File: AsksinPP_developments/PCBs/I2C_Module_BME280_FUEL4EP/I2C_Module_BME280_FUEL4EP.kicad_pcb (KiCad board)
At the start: 2 copper layers, 30.5 x 17 mm, 12 parts, among them J1 Conn_01x04, J2 Conn_01x04, U1 BME280

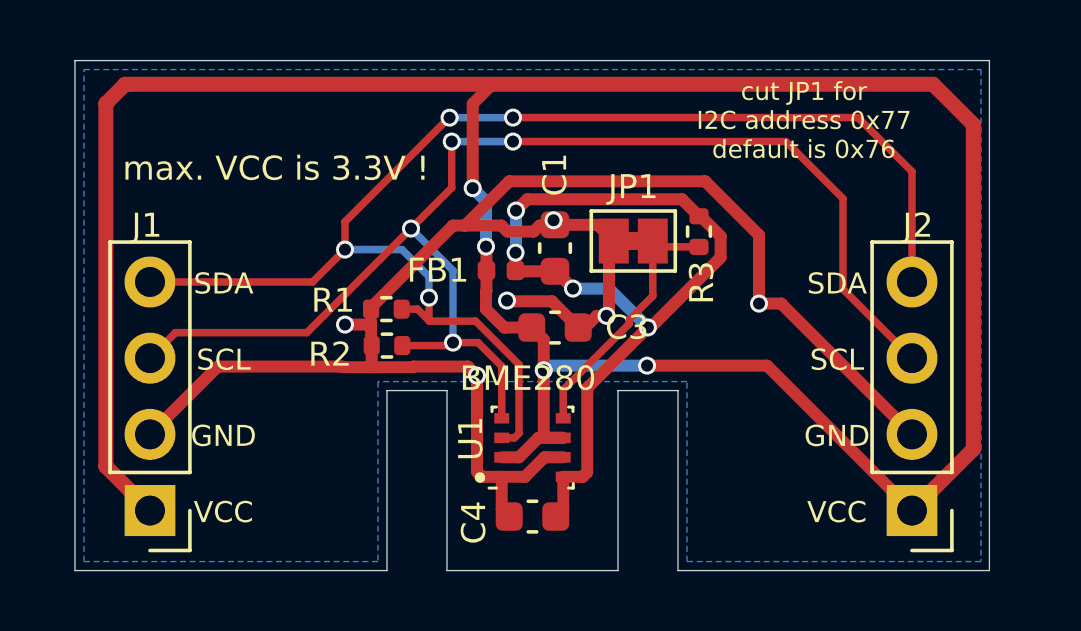
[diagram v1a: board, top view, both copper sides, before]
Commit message: PCB: I2C_Module_SHT85_BME280_FUEL4EP, I2C_Module_BME680_FUEL4EP: correction of connector placements in 3D view; 4Bit_I2C_Port_Expander_Module_FUEL4EP: change from 2N7000 to 2N7002K for SMD assembly
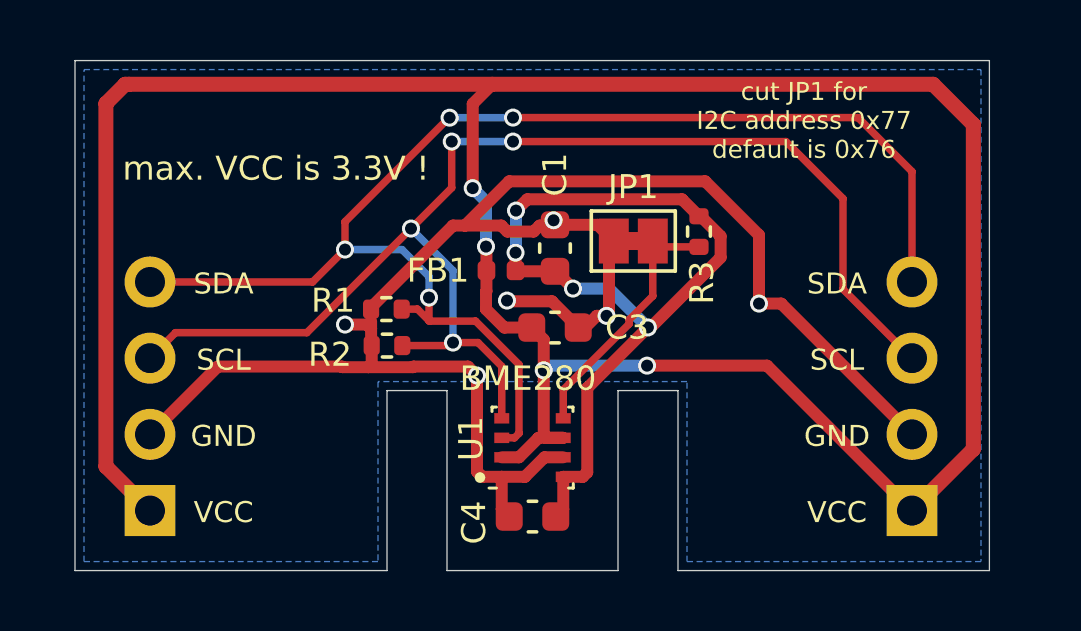
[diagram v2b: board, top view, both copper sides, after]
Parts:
- J1, J2: moved to B.Cu
- turned J1 to 0 degrees
- turned J2 to 0 degrees
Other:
- board text added: "BME280 I2C Modul (C) FUEL4EP V1.1 12/2023"
- board text removed: "BME280 I2C Modul (C) FUEL4EP V1.0 9/2023"

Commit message: PCBs: fix of I2C Pull-up resistors that were wrongly tied to GND
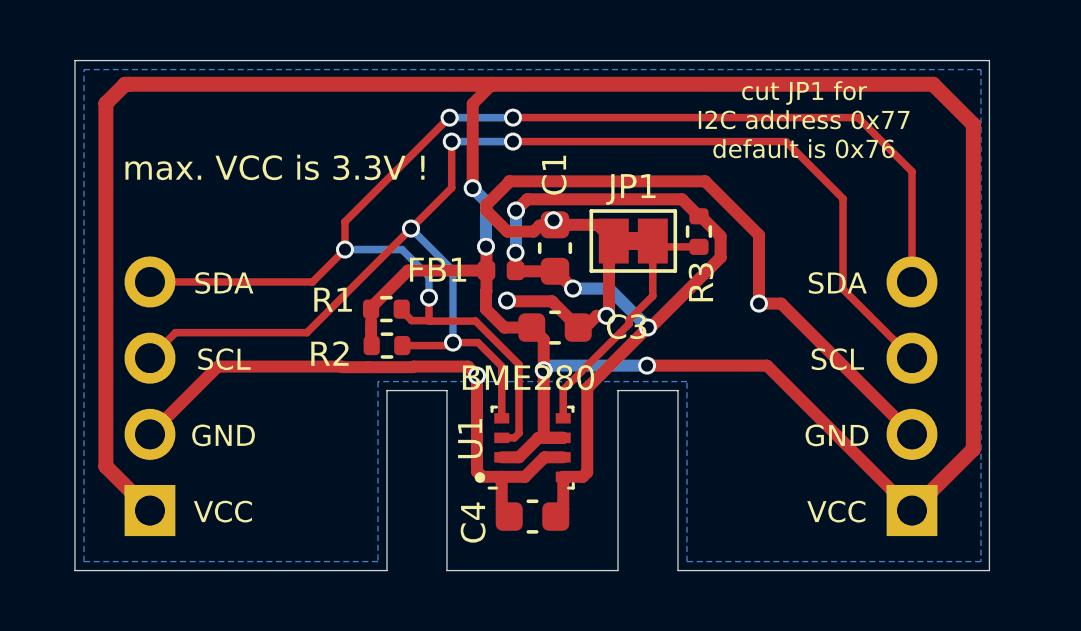
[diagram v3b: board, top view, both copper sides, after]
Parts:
- R1, R2: value 4.7k -> 10k
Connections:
- R1 pad 2: GND -> VCC
- R2 pad 2: GND -> VCC
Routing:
- net GND: track 58.0 -> 50.2 mm, vias 6 -> 5
- net VCC: track 88.5 -> 93.4 mm
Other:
- board text added: "BME280 I2C Modul (C) FUEL4EP V1.2 02/2024"
- board text removed: "BME280 I2C Modul (C) FUEL4EP V1.1 12/2023"
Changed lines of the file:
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@@
   (title_block
     (title "I2C_Module_BME280_FUEL4EP")
-    (date "2023-12-15")
-    (rev "V1.1")
+    (date "2024-02-08")
+    (rev "V1.2")
     (company "(c) FUEL4EP")
   )
@@
     (descr "Resistor SMD 0402 (1005 Metric), square (rectangular) end terminal, IPC_7351 nominal, (Body size source: IPC-SM-782 page 72, https://www.pcb-3d.com/wordpress/wp-content/uploads/ipc-sm-782a_amendment_1_and_2.pdf), generated with kicad-footprint-generator")
     (tags "resistor")
-    (property "LCSC" "C25900")
+    (property "LCSC" "C25744")
     (property "Sheetfile" "I2C_Module_BME280_FUEL4EP.kicad_sch")
     (property "Sheetname" "")
@@
       (effects (font (size 0.8 0.8) (thickness 0.15)))
     )
-    (fp_text value "4.7k" (at -0.12 -0.015) (layer "F.Fab")
+    (fp_text value "10k" (at -0.12 -0.015) (layer "F.Fab")
       (effects (font (size 0.8 0.8) (thickness 0.15)))
     )
@@
       (net 4 "/SDA") (pintype "passive"))
     (pad "2" smd roundrect (at 0.51 0 180) (size 0.54 0.64) (layers "F.Cu" "F.Paste" "F.Mask") (roundrect_rratio 0.25)
-      (net 2 "GND") (pintype "passive"))
+      (net 1 "VCC") (pintype "passive"))
     (model "${KICAD6_3DMODEL_DIR}/Resistor_SMD.3dshapes/R_0402_1005Metric.wrl"
       (offset (xyz 0 0 0))
@@
     (descr "Resistor SMD 0402 (1005 Metric), square (rectangular) end terminal, IPC_7351 nominal, (Body size source: IPC-SM-782 page 72, https://www.pcb-3d.com/wordpress/wp-content/uploads/ipc-sm-782a_amendment_1_and_2.pdf), generated with kicad-footprint-generator")
     (tags "resistor")
-    (property "LCSC" "C25900")
+    (property "LCSC" "C25744")
     (property "Sheetfile" "I2C_Module_BME280_FUEL4EP.kicad_sch")
     (property "Sheetname" "")
@@
       (effects (font (size 0.8 0.8) (thickness 0.15)))
     )
-    (fp_text value "4.7k" (at -0.2 -0.1) (layer "F.Fab")
+    (fp_text value "10k" (at -0.2 -0.1) (layer "F.Fab")
       (effects (font (size 0.8 0.8) (thickness 0.15)))
     )
@@
       (net 3 "/SCL") (pintype "passive"))
     (pad "2" smd roundrect (at 0.51 0 180) (size 0.54 0.64) (layers "F.Cu" "F.Paste" "F.Mask") (roundrect_rratio 0.25)
-      (net 2 "GND") (pintype "passive"))
+      (net 1 "VCC") (pintype "passive"))
     (model "${KICAD6_3DMODEL_DIR}/Resistor_SMD.3dshapes/R_0402_1005Metric.wrl"
       (offset (xyz 0 0 0))
@@
   (gr_line (start 18.1 -6) (end 18.1 0) (layer "Edge.Cuts") (width 0.0381))
   (gr_line (start 30.48 -17) (end 30.48 0) (layer "Edge.Cuts") (width 0.0381))
-  (gr_text "BME280\nI2C Modul\n(C) FUEL4EP\nV1.1\n12/2023" (at 15.1 -9.2) (layer "B.SilkS")
+  (gr_text "BME280\nI2C Modul\n(C) FUEL4EP\nV1.2\n02/2024" (at 15.1 -9.2) (layer "B.SilkS")
     (effects (font (size 0.7 0.7) (thickness 0.1524)) (justify mirror))
   )
@@
   (segment (start 1.672685 -16.21) (end 1.8 -16.21) (width 0.5) (layer "F.Cu") (net 1))
   (segment (start 15.45 -4.425) (end 14.8 -3.775) (width 0.4) (layer "F.Cu") (net 1))
+  (segment (start 9.87 -8.771604) (end 11.098396 -10) (width 0.4) (layer "F.Cu") (net 1))
   (segment (start 29.945 -4.045) (end 29.945 -14.868858) (width 0.5) (layer "F.Cu") (net 1))
   (segment (start 23.068742 -6.831258) (end 19.068742 -6.831258) (width 0.4) (layer "F.Cu") (net 1))
@@
   (segment (start 1.8 -16.21) (end 13.91 -16.21) (width 0.5) (layer "F.Cu") (net 1))
   (segment (start 13.7005 -8.710257) (end 14.310757 -8.1) (width 0.4) (layer "F.Cu") (net 1))
+  (segment (start 9.87 -8.315) (end 9.87 -8.07) (width 0.4) (layer "F.Cu") (net 1))
   (segment (start 13.91 -16.21) (end 28.603858 -16.21) (width 0.5) (layer "F.Cu") (net 1))
   (segment (start 29.945 -14.868858) (end 28.603858 -16.21) (width 0.5) (layer "F.Cu") (net 1))
+  (segment (start 11.098396 -10) (end 13.715 -10) (width 0.4) (layer "F.Cu") (net 1))
   (segment (start 13.7005 -9.289743) (end 13.7005 -8.710257) (width 0.4) (layer "F.Cu") (net 1))
   (segment (start 13.715 -10) (end 13.715 -9.304243) (width 0.4) (layer "F.Cu") (net 1))
+  (segment (start 9.87 -8.715) (end 9.87 -8.771604) (width 0.4) (layer "F.Cu") (net 1))
   (segment (start 15.625 -4.5) (end 15.625 -7.7) (width 0.4) (layer "F.Cu") (net 1))
   (segment (start 27.9 -2) (end 23.068742 -6.831258) (width 0.4) (layer "F.Cu") (net 1))
+  (segment (start 9.87 -8.07) (end 9.87 -7.77) (width 0.4) (layer "F.Cu") (net 1))
   (segment (start 13.715 -10) (end 13.715 -10.785) (width 0.4) (layer "F.Cu") (net 1))
   (segment (start 27.9 -2) (end 29.945 -4.045) (width 0.5) (layer "F.Cu") (net 1))
@@
   (segment (start 14.425 -8.975) (end 15.9 -8.975) (width 0.4) (layer "F.Cu") (net 2))
   (segment (start 14.225 -2.05) (end 14.475 -1.8) (width 0.4) (layer "F.Cu") (net 2))
+  (segment (start 13.716 -11.994757) (end 14.410257 -11.3005) (width 0.4) (layer "F.Cu") (net 2))
   (segment (start 13.575 -3.125) (end 13.4 -3.3) (width 0.4) (layer "F.Cu") (net 2))
   (segment (start 15.489743 -11.5005) (end 15.289743 -11.3005) (width 0.4) (layer "F.Cu") (net 2))
   (segment (start 21.007104 -12.9745) (end 14.472896 -12.9745) (width 0.4) (layer "F.Cu") (net 2))
-  (segment (start 12.598896 -11.5005) (end 9.87 -8.771604) (width 0.4) (layer "F.Cu") (net 2))
   (segment (start 17.8 -8.572728) (end 17.719014 -8.491742) (width 0.4) (layer "F.Cu") (net 2))
+  (segment (start 14.472896 -12.948896) (end 13.716 -12.192) (width 0.4) (layer "F.Cu") (net 2))
   (segment (start 13.4 -3.3) (end 13.4 -6.5) (width 0.4) (layer "F.Cu") (net 2))
   (segment (start 14.425 -8.975) (end 14.4 -9) (width 0.4) (layer "F.Cu") (net 2))
@@
   (segment (start 8.92 -6.78) (end 8.9 -6.8) (width 0.4) (layer "F.Cu") (net 2))
   (segment (start 17.391742 -8.491742) (end 17.719014 -8.491742) (width 0.4) (layer "F.Cu") (net 2))
+  (segment (start 14.472896 -12.9745) (end 14.472896 -12.948896) (width 0.4) (layer "F.Cu") (net 2))
   (segment (start 15.9755 -11.5005) (end 15.489743 -11.5005) (width 0.4) (layer "F.Cu") (net 2))
   (segment (start 13.4 -6.5) (end 13.1 -6.8) (width 0.4) (layer "F.Cu") (net 2))
-  (segment (start 14.472896 -12.9745) (end 12.998896 -11.5005) (width 0.4) (layer "F.Cu") (net 2))
   (segment (start 8.9 -6.8) (end 4.76 -6.8) (width 0.4) (layer "F.Cu") (net 2))
   (segment (start 14.225 -3.125) (end 14.225 -2.05) (width 0.4) (layer "F.Cu") (net 2))
   (segment (start 17 -8.1) (end 17.391742 -8.491742) (width 0.4) (layer "F.Cu") (net 2))
-  (segment (start 9.87 -8.315) (end 9.87 -8.07) (width 0.4) (layer "F.Cu") (net 2))
-  (segment (start 9.89 -6.89) (end 9.78 -6.78) (width 0.4) (layer "F.Cu") (net 2))
-  (segment (start 9.89 -7.5) (end 9.89 -6.89) (width 0.4) (layer "F.Cu") (net 2))
   (segment (start 23.54 -8.9) (end 22.8 -8.9) (width 0.4) (layer "F.Cu") (net 2))
   (segment (start 16.775 -8.1) (end 15.9 -8.975) (width 0.4) (layer "F.Cu") (net 2))
-  (segment (start 9 -8.2) (end 9.74 -8.2) (width 0.4) (layer "F.Cu") (net 2))
-  (segment (start 9.87 -8.07) (end 9.87 -7.77) (width 0.4) (layer "F.Cu") (net 2))
-  (segment (start 9.74 -8.2) (end 9.87 -8.07) (width 0.4) (layer "F.Cu") (net 2))
-  (segment (start 14.410257 -11.3005) (end 14.210257 -11.5005) (width 0.4) (layer "F.Cu") (net 2))
-  (segment (start 12.998896 -11.5005) (end 12.598896 -11.5005) (width 0.4) (layer "F.Cu") (net 2))
   (segment (start 13.1 -6.8) (end 11.286604 -6.8) (width 0.4) (layer "F.Cu") (net 2))
-  (segment (start 14.210257 -11.5005) (end 12.998896 -11.5005) (width 0.4) (layer "F.Cu") (net 2))
   (segment (start 4.76 -6.8) (end 2.5 -4.54) (width 0.4) (layer "F.Cu") (net 2))
   (segment (start 11.286604 -6.8) (end 11.266604 -6.78) (width 0.4) (layer "F.Cu") (net 2))
@@
   (segment (start 11.266604 -6.78) (end 9.78 -6.78) (width 0.4) (layer "F.Cu") (net 2))
   (segment (start 15.289743 -11.3005) (end 14.410257 -11.3005) (width 0.4) (layer "F.Cu") (net 2))
+  (segment (start 13.716 -12.192) (end 13.716 -11.994757) (width 0.4) (layer "F.Cu") (net 2))
   (segment (start 27.9 -4.54) (end 23.54 -8.9) (width 0.4) (layer "F.Cu") (net 2))
   (via (at 15.952178 -11.6755) (size 0.6) (drill 0.4) (layers "F.Cu" "B.Cu") (net 2))
-  (via (at 9 -8.2) (size 0.6) (drill 0.4) (layers "F.Cu" "B.Cu") (net 2))
   (via (at 17.719014 -8.491742) (size 0.6) (drill 0.4) (layers "F.Cu" "B.Cu") (net 2))
   (via (at 13.4 -6.5) (size 0.6) (drill 0.4) (layers "F.Cu" "B.Cu") (net 2))
@@
   (segment (start 2.5 -9.62) (end 7.92 -9.62) (width 0.25) (layer "F.Cu") (net 4))
   (segment (start 11.8 -9.1) (end 11.8 -8.33) (width 0.25) (layer "F.Cu") (net 4))
+  (segment (start 11.228 -8.33) (end 11.8 -8.33) (width 0.25) (layer "F.Cu") (net 4))
   (segment (start 7.92 -9.62) (end 9 -10.7) (width 0.25) (layer "F.Cu") (net 4))
   (segment (start 27.9 -9.62) (end 27.9 -13.3) (width 0.25) (layer "F.Cu") (net 4))
@@
   (segment (start 26.100497 -15.099503) (end 14.6 -15.099503) (width 0.25) (layer "F.Cu") (net 4))
   (segment (start 12.470408 -15.096368) (end 12.486493 -15.096368) (width 0.25) (layer "F.Cu") (net 4))
+  (segment (start 10.89 -8.715) (end 10.89 -8.668) (width 0.25) (layer "F.Cu") (net 4))
   (segment (start 9 -11.62596) (end 12.470408 -15.096368) (width 0.25) (layer "F.Cu") (net 4))
   (segment (start 14.8 -4.575) (end 14.8 -6.869001) (width 0.25) (layer "F.Cu") (net 4))
-  (segment (start 11.415 -8.715) (end 10.89 -8.715) (width 0.25) (layer "F.Cu") (net 4))
   (segment (start 14.8 -6.869001) (end 13.354001 -8.315) (width 0.25) (layer "F.Cu") (net 4))
+  (segment (start 10.89 -8.668) (end 11.228 -8.33) (width 0.25) (layer "F.Cu") (net 4))
   (segment (start 14.65 -4.425) (end 14.8 -4.575) (width 0.25) (layer "F.Cu") (net 4))
   (segment (start 9 -10.7) (end 9 -11.62596) (width 0.25) (layer "F.Cu") (net 4))
-  (segment (start 11.815 -8.315) (end 11.415 -8.715) (width 0.25) (layer "F.Cu") (net 4))
   (via (at 9 -10.7) (size 0.6) (drill 0.4) (layers "F.Cu" "B.Cu") (net 4))
   (via (at 12.486493 -15.096368) (size 0.6) (drill 0.4) (layers "F.Cu" "B.Cu") (net 4))

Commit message: PCBs: upgrade some PCBs to KiCAD 7; fix of unnecessary leakage current of I2C address selector: I2C_Module_SHT85_BME280_FUEL4EP, I2C_Module_SHT45_BME280_small_FUEL4EP, I2C_Module_SHT45_BME280_FUEL4EP, I2C_Module_BME280_FUEL4EP, and I2C_Module_BME680_FUEL4EP
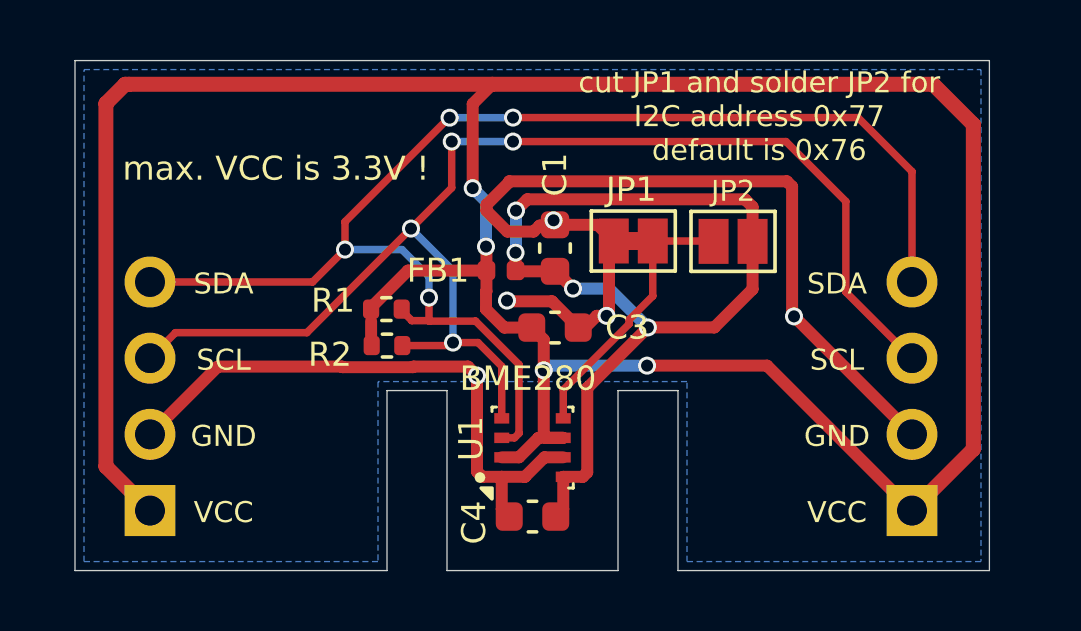
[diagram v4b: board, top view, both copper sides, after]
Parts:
- removed R3: 10k, Resistor_SMD:R_0402_1005Metric
- added JP2: SolderJumper_2_Open, Jumper:SolderJumper-2_P1.3mm_Open_Pad1.0x1.5mm, F.Cu at (21.9, -11.0)
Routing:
- net VDDA: track 26.7 -> 30.0 mm
- net GND: track 50.2 -> 51.3 mm
- net Net-(JP1-B): track 8.49 -> 9.16 mm
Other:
- board text added: "BME280 I2C Modul (C) FUEL4EP V1.3 04/2024"
- board text added: "cut JP1 and solder JP2 for I2C address 0x77 default is 0x76"
- board text removed: "BME280 I2C Modul (C) FUEL4EP V1.2 02/2024"
- board text removed: "cut JP1 for I2C address 0x77 default is 0x76"

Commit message: PCBs/I2C_Module_SHT45_BME280_FUEL4EP und PCBs/I2C_Module_BME280_FUEL4EP: migration to KiCAD 8; fix of DRC rules for PCBs/I2C_Module_SHT45_BME280_FUEL4EP
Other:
- board text added: "BME280 I2C Modul (C) FUEL4EP V1.4 09/2024"
- board text removed: "BME280 I2C Modul (C) FUEL4EP V1.3 04/2024"
